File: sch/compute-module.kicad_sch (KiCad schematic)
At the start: 10 parts, among them J2 SAM10346-ND, J3 Conn_02x20_Odd_Even, M1 ComputeModule5-CM5, SW1 1825910-6

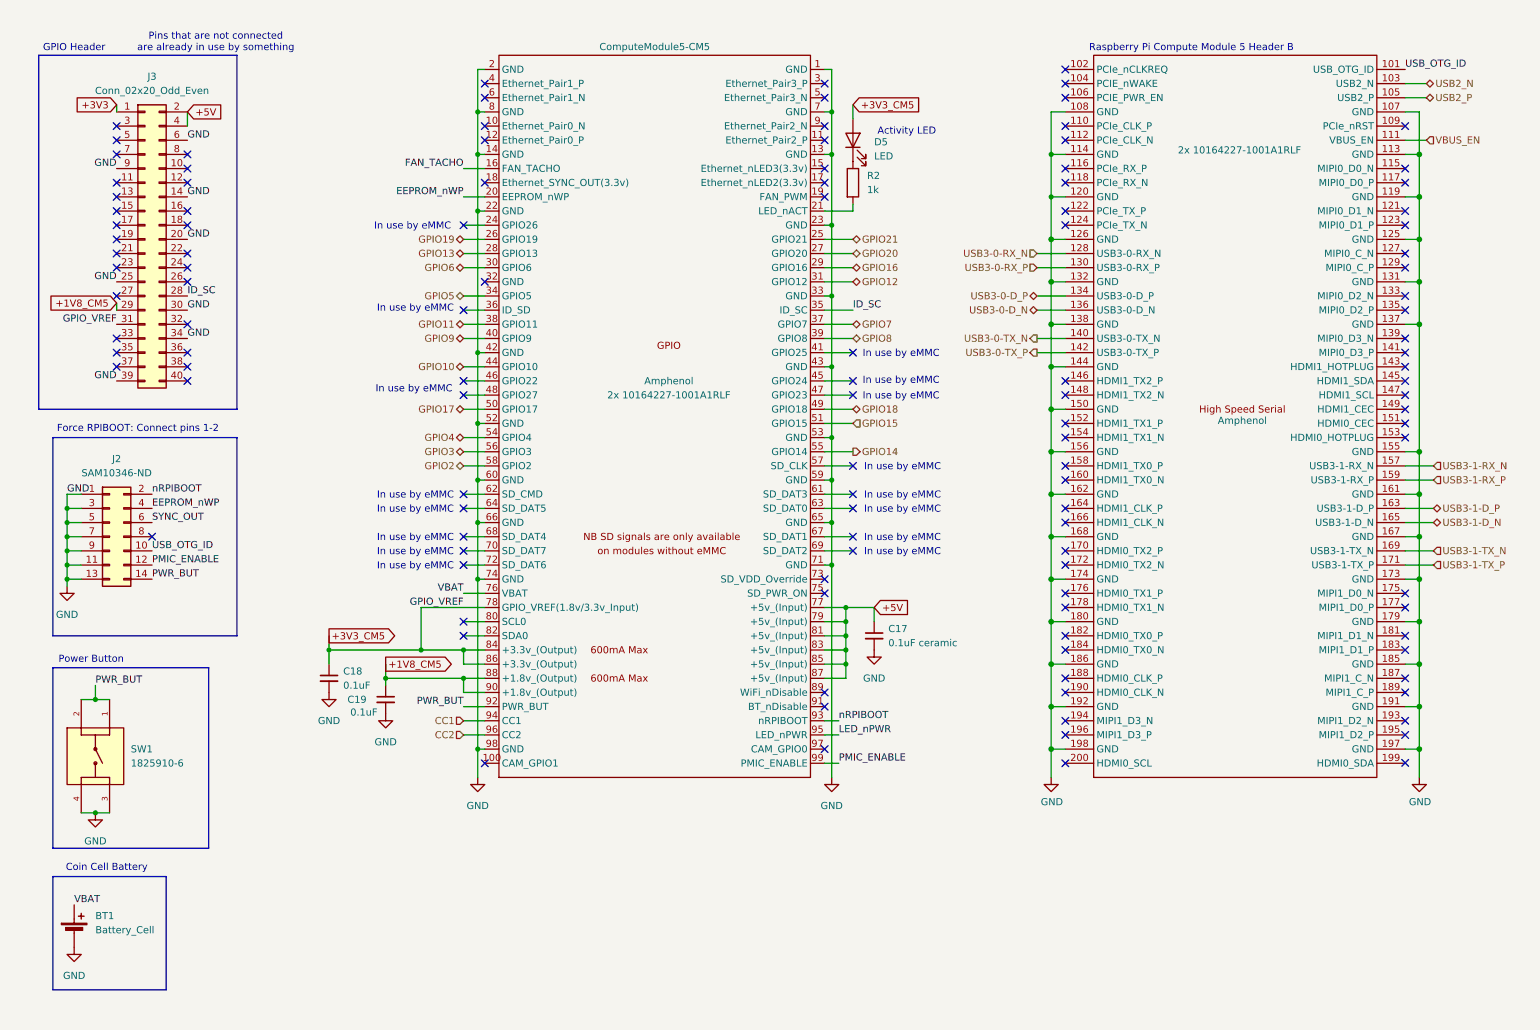
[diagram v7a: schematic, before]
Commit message: Endret nummereringer komponenter
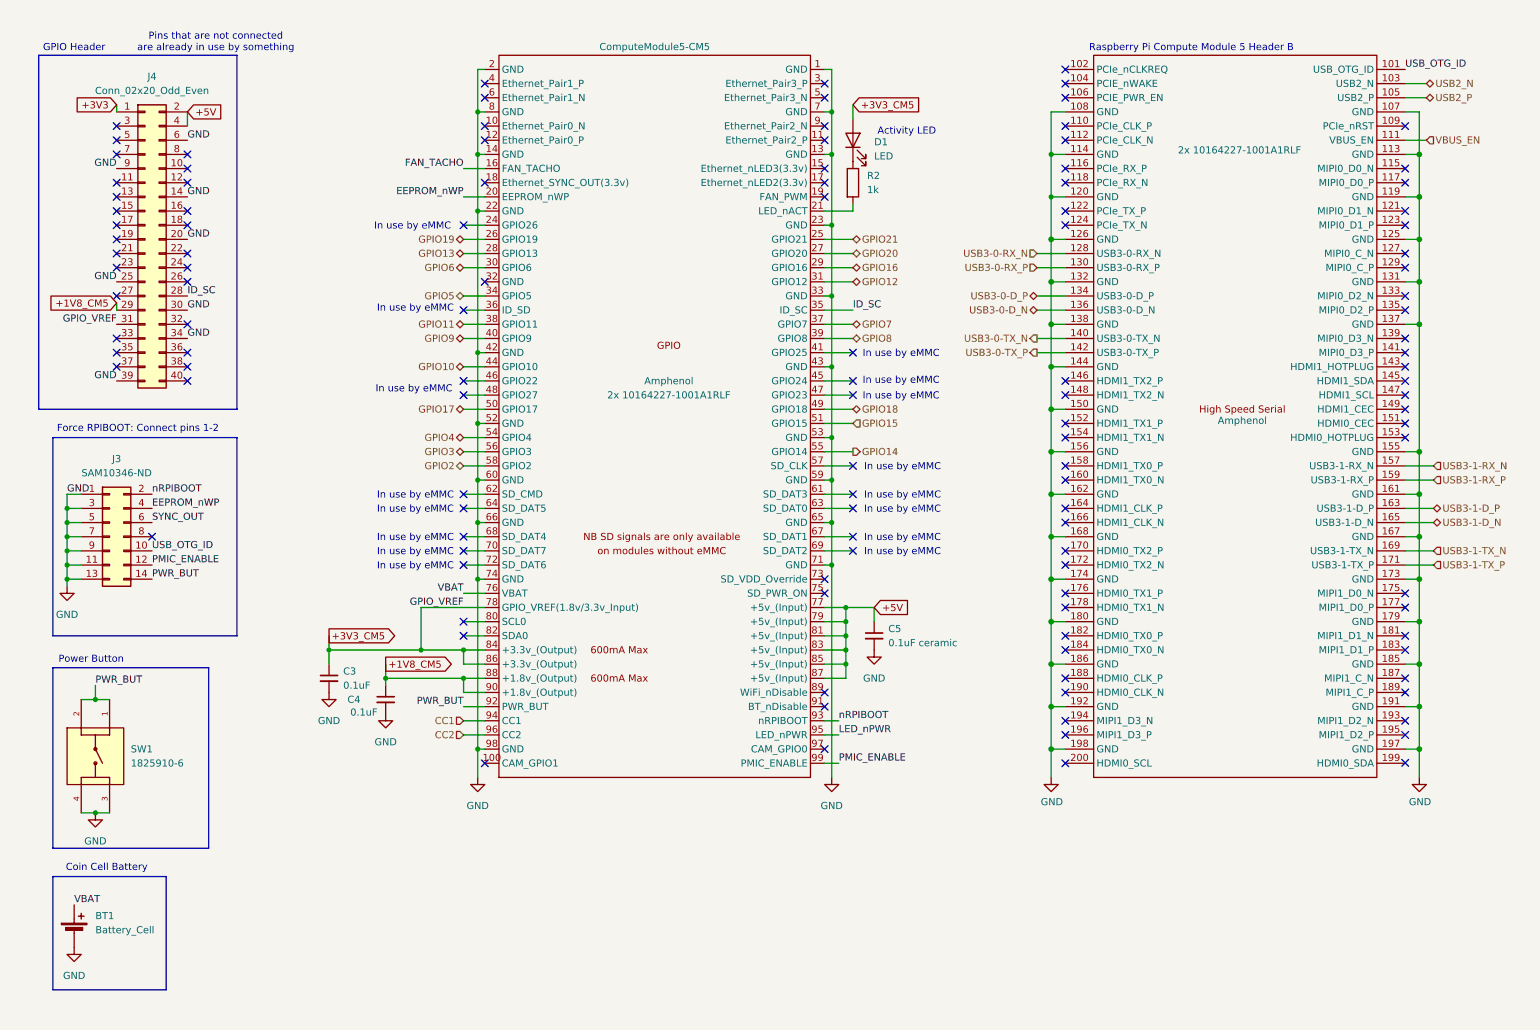
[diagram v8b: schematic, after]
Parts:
- renumbered C18 to C3, C19 to C4, C17 to C5, D5 to D1, J2 to J3, J3 to J4
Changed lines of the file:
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@@
 		(on_board yes)
 		(dnp no)
-		(property "Reference" "#PWR014"
+		(property "Reference" "#PWR017"
 			(at 265.43 158.75 0)
 			(effects
@@
 			(project "audiograb"
 				(path "/c46c2311-6d4b-411d-b012-c7730eac136d/75b669f4-4784-4707-8d6c-b4da66be0510"
-					(reference "#PWR014")
+					(reference "#PWR017")
 					(unit 1)
 				)
@@
 		(on_board yes)
 		(dnp no)
-		(property "Reference" "#PWR013"
+		(property "Reference" "#PWR016"
 			(at 199.39 158.75 0)
 			(effects
@@
 			(project "audiograb"
 				(path "/c46c2311-6d4b-411d-b012-c7730eac136d/75b669f4-4784-4707-8d6c-b4da66be0510"
-					(reference "#PWR013")
+					(reference "#PWR016")
 					(unit 1)
 				)
@@
 		(dnp no)
 		(fields_autoplaced yes)
-		(property "Reference" "#PWR064"
+		(property "Reference" "#PWR015"
 			(at 167.64 135.89 0)
 			(effects
@@
 			(project "audiograb"
 				(path "/c46c2311-6d4b-411d-b012-c7730eac136d/75b669f4-4784-4707-8d6c-b4da66be0510"
-					(reference "#PWR064")
+					(reference "#PWR015")
 					(unit 1)
 				)
@@
 		(dnp no)
 		(fields_autoplaced yes)
-		(property "Reference" "J3"
+		(property "Reference" "J4"
 			(at 38.1 26.67 0)
 			(effects
@@
 			(project ""
 				(path "/c46c2311-6d4b-411d-b012-c7730eac136d/75b669f4-4784-4707-8d6c-b4da66be0510"
-					(reference "J3")
+					(reference "J4")
 					(unit 1)
 				)
@@
 		(on_board yes)
 		(dnp no)
-		(property "Reference" "#PWR09"
+		(property "Reference" "#PWR013"
 			(at 96.52 158.75 0)
 			(effects
@@
 			(project "audiograb"
 				(path "/c46c2311-6d4b-411d-b012-c7730eac136d/75b669f4-4784-4707-8d6c-b4da66be0510"
-					(reference "#PWR09")
+					(reference "#PWR013")
 					(unit 1)
 				)
@@
 		(dnp no)
 		(fields_autoplaced yes)
-		(property "Reference" "#PWR010"
+		(property "Reference" "#PWR09"
 			(at 24.13 189.23 0)
 			(effects
@@
 			(project ""
 				(path "/c46c2311-6d4b-411d-b012-c7730eac136d/75b669f4-4784-4707-8d6c-b4da66be0510"
-					(reference "#PWR010")
+					(reference "#PWR09")
 					(unit 1)
 				)
@@
 		(dnp no)
 		(fields_autoplaced yes)
-		(property "Reference" "#PWR065"
+		(property "Reference" "#PWR011"
 			(at 69.85 143.51 0)
 			(effects
@@
 			(project "audiograb"
 				(path "/c46c2311-6d4b-411d-b012-c7730eac136d/75b669f4-4784-4707-8d6c-b4da66be0510"
-					(reference "#PWR065")
+					(reference "#PWR011")
 					(unit 1)
 				)
@@
 		(dnp no)
 		(fields_autoplaced yes)
-		(property "Reference" "C18"
+		(property "Reference" "C3"
 			(at 72.39 133.3562 0)
 			(effects
@@
 			(project "audiograb"
 				(path "/c46c2311-6d4b-411d-b012-c7730eac136d/75b669f4-4784-4707-8d6c-b4da66be0510"
-					(reference "C18")
+					(reference "C3")
 					(unit 1)
 				)
@@
 		(dnp no)
 		(fields_autoplaced yes)
-		(property "Reference" "#PWR066"
+		(property "Reference" "#PWR012"
 			(at 80.01 147.32 0)
 			(effects
@@
 			(project "audiograb"
 				(path "/c46c2311-6d4b-411d-b012-c7730eac136d/75b669f4-4784-4707-8d6c-b4da66be0510"
-					(reference "#PWR066")
+					(reference "#PWR012")
 					(unit 1)
 				)
@@
 		(dnp no)
 		(fields_autoplaced yes)
-		(property "Reference" "C17"
+		(property "Reference" "C5"
 			(at 170.18 125.7362 0)
 			(effects
@@
 			(project "audiograb"
 				(path "/c46c2311-6d4b-411d-b012-c7730eac136d/75b669f4-4784-4707-8d6c-b4da66be0510"
-					(reference "C17")
+					(reference "C5")
 					(unit 1)
 				)
@@
 		(dnp no)
 		(fields_autoplaced yes)
-		(property "Reference" "J2"
+		(property "Reference" "J3"
 			(at 31.75 95.25 0)
 			(effects
@@
 			(project ""
 				(path "/c46c2311-6d4b-411d-b012-c7730eac136d/75b669f4-4784-4707-8d6c-b4da66be0510"
-					(reference "J2")
+					(reference "J3")
 					(unit 1)
 				)
@@
 		(dnp no)
 		(fields_autoplaced yes)
-		(property "Reference" "D5"
+		(property "Reference" "D1"
 			(at 167.64 38.4174 90)
 			(effects
@@
 			(project "audiograb"
 				(path "/c46c2311-6d4b-411d-b012-c7730eac136d/75b669f4-4784-4707-8d6c-b4da66be0510"
-					(reference "D5")
+					(reference "D1")
 					(unit 1)
 				)
@@
 		(dnp no)
 		(fields_autoplaced yes)
-		(property "Reference" "#PWR012"
+		(property "Reference" "#PWR014"
 			(at 160.02 158.75 0)
 			(effects
@@
 			(project "audiograb"
 				(path "/c46c2311-6d4b-411d-b012-c7730eac136d/75b669f4-4784-4707-8d6c-b4da66be0510"
-					(reference "#PWR012")
+					(reference "#PWR014")
 					(unit 1)
 				)
@@
 		(dnp no)
 		(fields_autoplaced yes)
-		(property "Reference" "#PWR011"
+		(property "Reference" "#PWR010"
 			(at 27.94 165.1 0)
 			(effects
@@
 			(project ""
 				(path "/c46c2311-6d4b-411d-b012-c7730eac136d/75b669f4-4784-4707-8d6c-b4da66be0510"
-					(reference "#PWR011")
+					(reference "#PWR010")
 					(unit 1)
 				)
@@
 		(on_board yes)
 		(dnp no)
-		(property "Reference" "C19"
+		(property "Reference" "C4"
 			(at 73.152 138.43 0)
 			(effects
@@
 			(project "audiograb"
 				(path "/c46c2311-6d4b-411d-b012-c7730eac136d/75b669f4-4784-4707-8d6c-b4da66be0510"
-					(reference "C19")
+					(reference "C4")
 					(unit 1)
 				)
